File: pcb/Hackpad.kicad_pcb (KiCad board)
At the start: 2 copper layers, 66 x 87 mm, 21 parts, among them J1 OLED_DISPLAY, SW1 SW_Push, SW2 SW_Push, SW3 SW_Push, SW4 SW_Push, SW5 SW_Push, SW6 SW_Push, SW7 RotaryEncoder_Switch, U1 MOUDLE-SEEEDUINO-XIAO

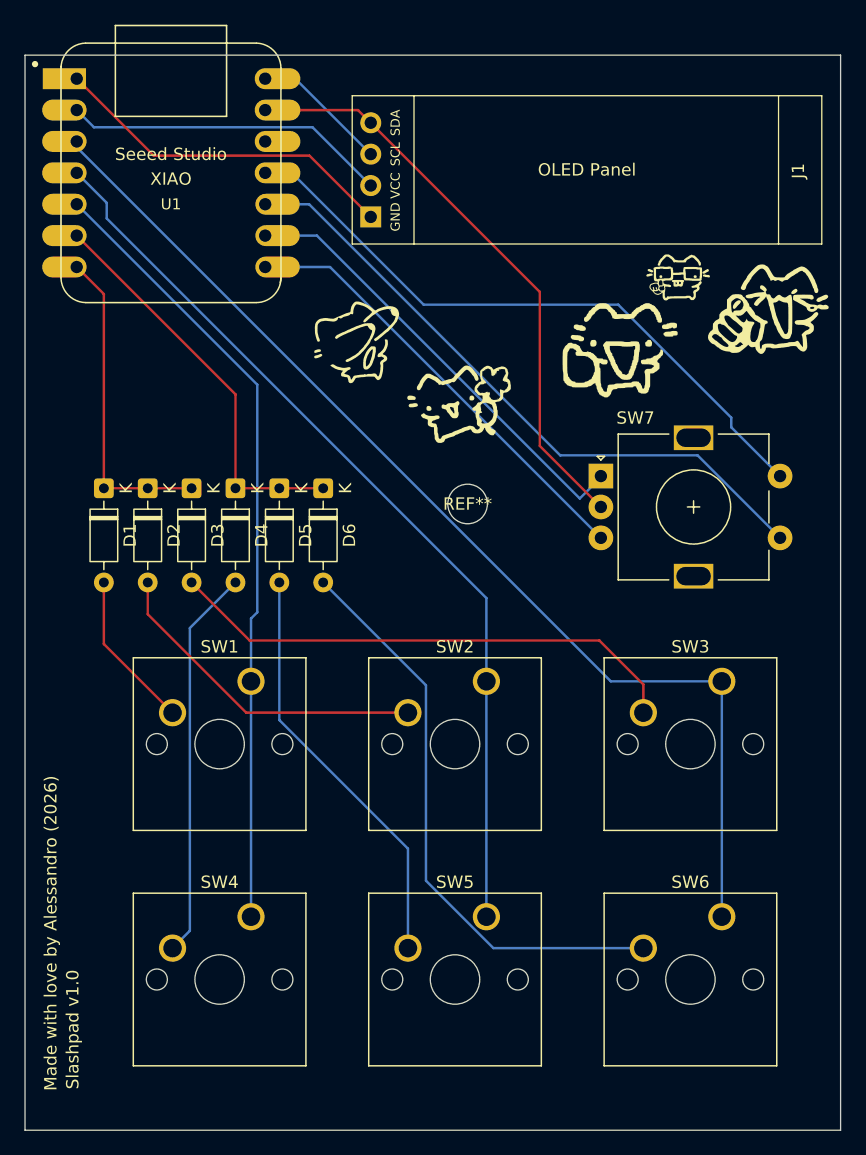
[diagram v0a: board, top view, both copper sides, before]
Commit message: Fixes + Adding new files
- Added new cats on the PCB
- Adjusted the PCB and routed everything again
- Adjusted the schematic
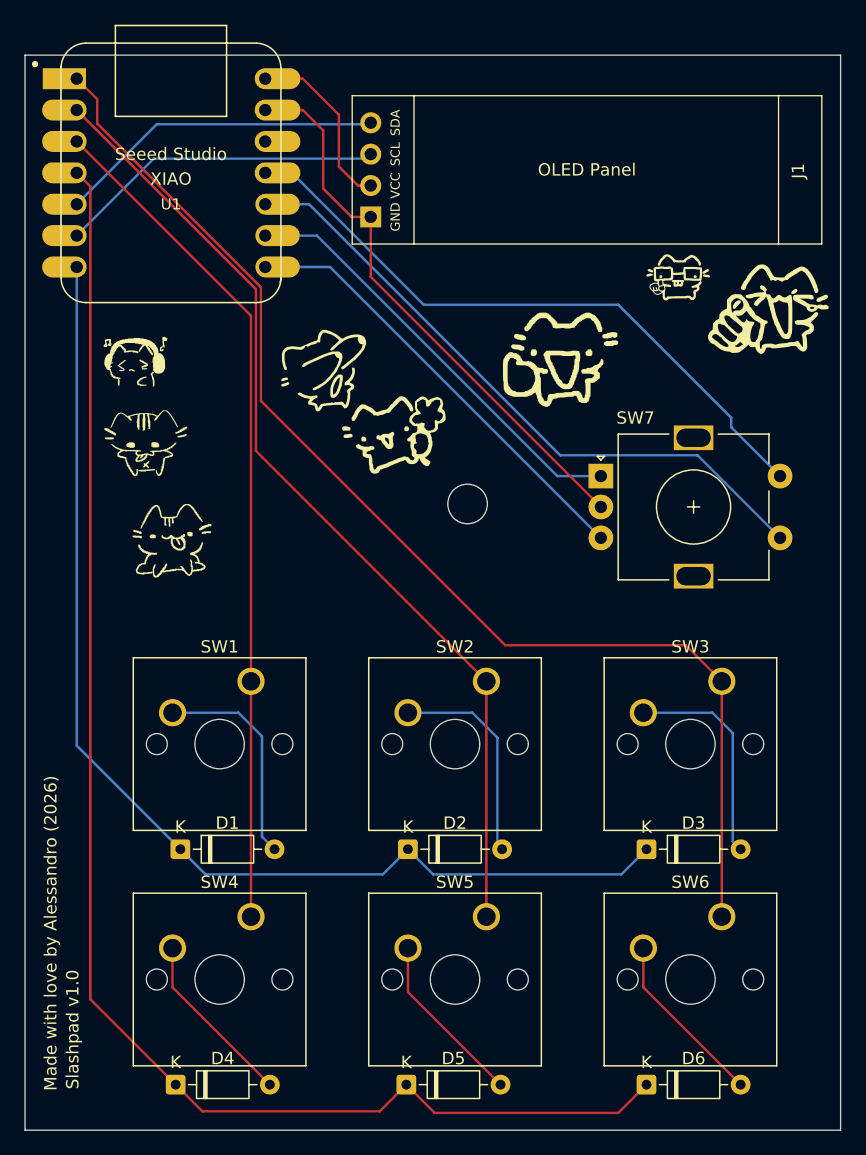
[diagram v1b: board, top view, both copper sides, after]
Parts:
- added G***: LOGO, 3DModelLibrary:cat8, F.Cu at (82.2, 79.9)
- added G***: LOGO, 3DModelLibrary:cat6, F.Cu at (79.5, 65.3)
- added G***: LOGO, 3DModelLibrary:cat7, F.Cu at (79.9, 71.4)
- moved D6 54.9 mm to (120.3, 122.9), turned to 0 degrees
- moved D5 49.3 mm to (100.8, 122.9), turned to 0 degrees
- moved D4 48.5 mm to (82.2, 122.9), turned to 0 degrees
- moved D3 47.0 mm to (120.3, 103.9), turned to 0 degrees
- moved D2 36.0 mm to (101.0, 103.9), turned to 0 degrees
- moved D1 29.9 mm to (82.5, 103.9), turned to 0 degrees
- moved G*** 5.83 mm to (99.9, 69.8)
- moved G*** 4.89 mm to (113.3, 64.1)
- moved G*** 3.51 mm to (94.5, 65.0)
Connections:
- J1 pad 1: SDA -> GND
- J1 pad 2: SCL -> VCC
- J1 pad 3: VCC -> SCL
- J1 pad 4: GND -> SDA
- U1 pad 1: SDA -> COL2
- U1 pad 2: SCL -> COL1
- U1 pad 3: COL2 -> COL0
- U1 pad 4: COL1 -> ROW1
- U1 pad 5: COL0 -> SDA
- U1 pad 6: ROW1 -> SCL
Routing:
- net ROW1: track 32.9 -> 118.9 mm
- net ROW0: track 25.9 -> 91.7 mm
- net Net-(D6-A): track 47.4 -> 14.3 mm
- net Net-(D3-A): track 42.3 -> 17.6 mm
- net Net-(D5-A): track 33.9 -> 14.2 mm
- net Net-(D4-A): track 31.7 -> 14.3 mm
- net Net-(D2-A): track 26.9 -> 17.3 mm
- net COL2: track 89.6 -> 98.0 mm
- net COL1: track 73.9 -> 79.0 mm
- net Net-(D1-A): track 12.8 -> 17.6 mm
- net COL0: track 63.9 -> 68.6 mm
- net VCC: track 11.1 -> 14.6 mm
- net SDA: track 28.4 -> 26.5 mm
- net EC11A: track 36.9 -> 35.2 mm
- net GND: track 47.8 -> 46.1 mm

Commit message: Fixes and new files added
- Added .step files of the case
- Added .step file of the whole macropad
- Added the firmware
- Modified the readme.md
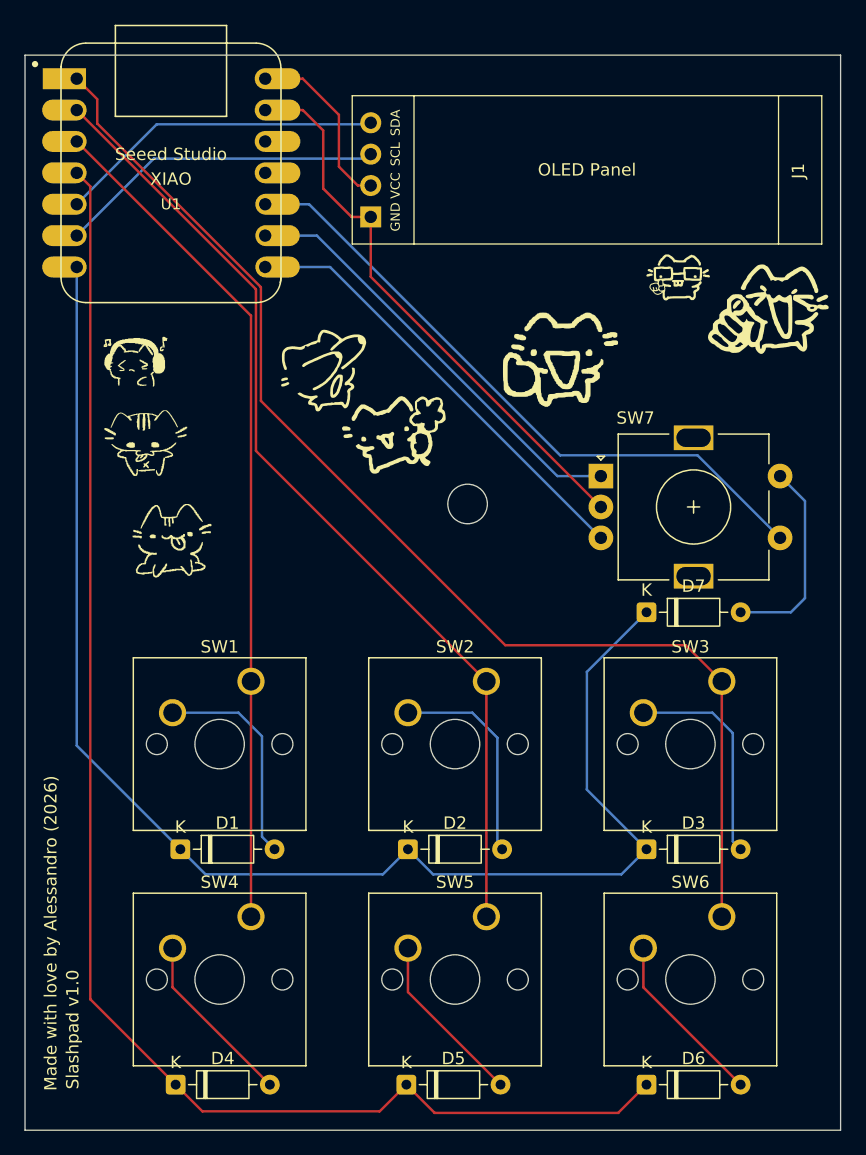
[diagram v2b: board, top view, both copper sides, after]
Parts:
- added D7: 1N4148, Diode_THT:D_DO-35_SOD27_P7.62mm_Horizontal, F.Cu at (120.3, 84.7)
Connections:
- net EC11S1 renamed COL3
- U1 pad 11: EC11S2 -> unconnected-(U1-PA6_A10_D10_MOSI-Pad11)
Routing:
- net EC11S2: track 52.3 -> 16.4 mm
- net ROW0: track 91.7 -> 114.9 mm
